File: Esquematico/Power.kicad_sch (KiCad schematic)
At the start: 5 parts, among them U1 AMS1117-3.3

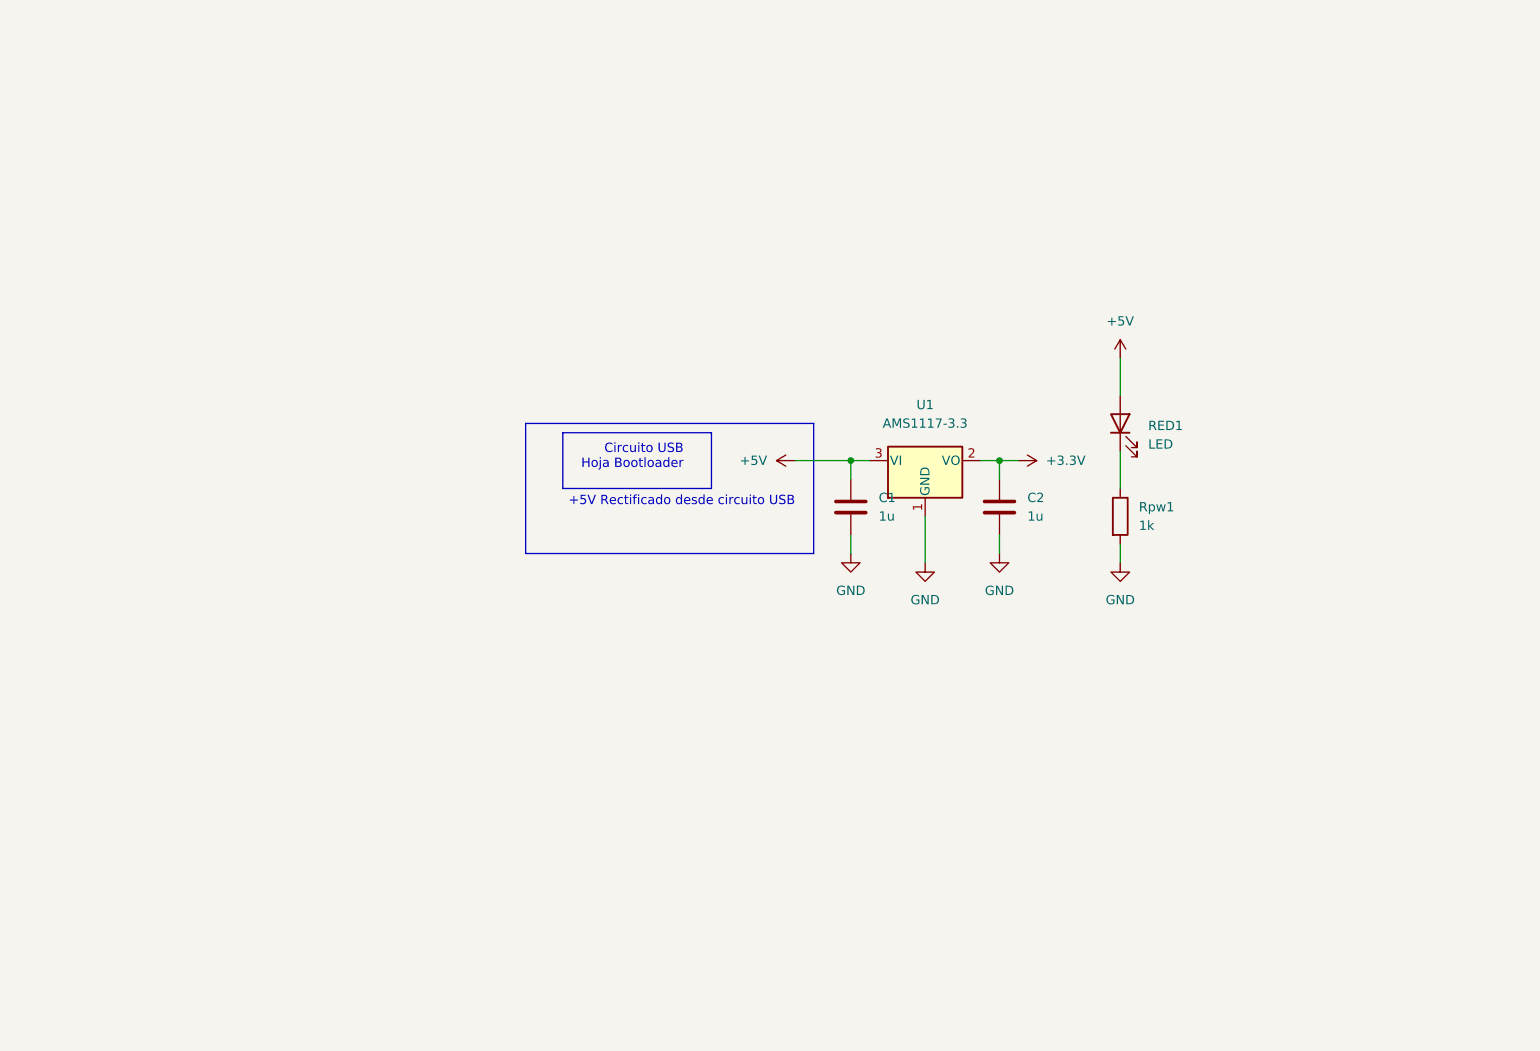
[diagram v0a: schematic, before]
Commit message: Agregado circuito de potencia a través de Jack y selector de posición para alimentar de USB, Jack o apagar
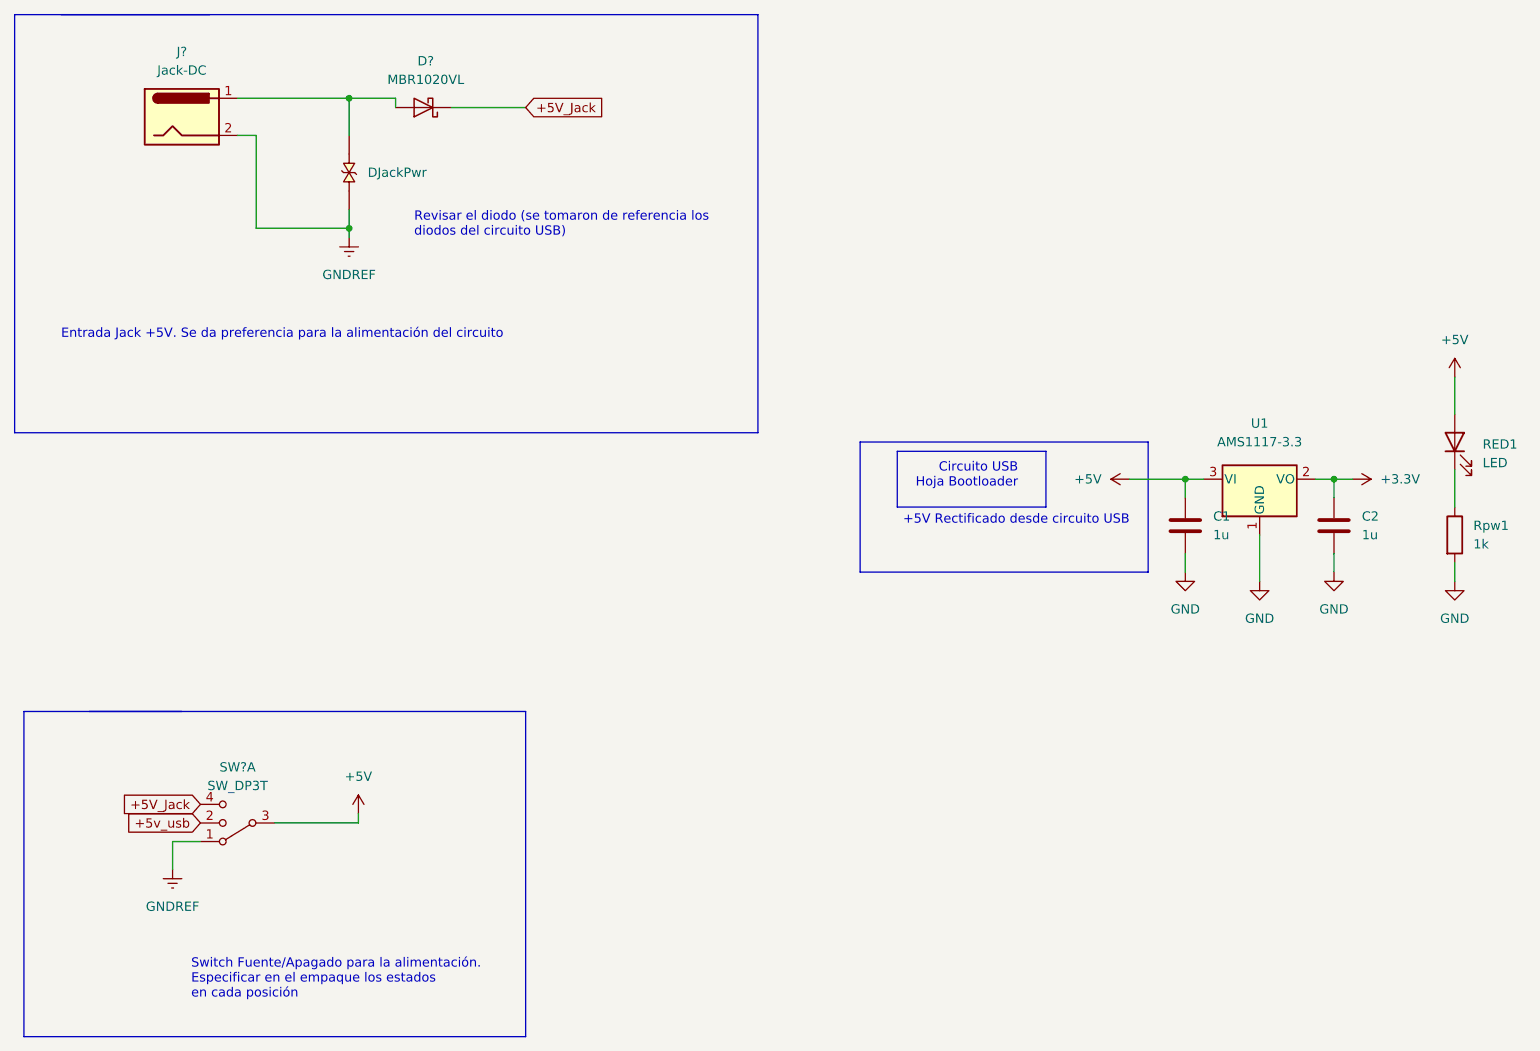
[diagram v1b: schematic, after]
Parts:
- added D?: MBR1020VL, Diode_SMD:D_SOD-123F, symbol Diode:MBR1020VL
- added DJackPwr: LESD5D5.0CT1G, TVS_LESD5D5.0CT1G, symbol LESD5D5.0CT1G:LESD5D5.0CT1G
- added J?: Jack-DC, symbol Connector:Jack-DC
- added SW?: SW_DP3T, symbol Switch:SW_DP3T
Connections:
- net +5V: now also SW?.3
- new net: D?.2 (A), DJackPwr.2, J?.1
- new net +5V_Jack: D?.1 (K), SW?.4
- new net +5v_usb: SW?.2
- new net GNDREF: DJackPwr.1, J?.2, SW?.1
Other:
- note added: "Entrada Jack +5V. Se da preferencia para la alimentación del circuito"
- note added: "Revisar el diodo (se tomaron de referencia los diodos del circuito USB)"
- note added: "Switch Fuente/Apagado para la alimentación. Especificar en el empaque los estados en cada posición"
- moved on the sheet: C1, C2, RED1, Rpw1, U1

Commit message: actualizacion huellas resitencias y capacitorees
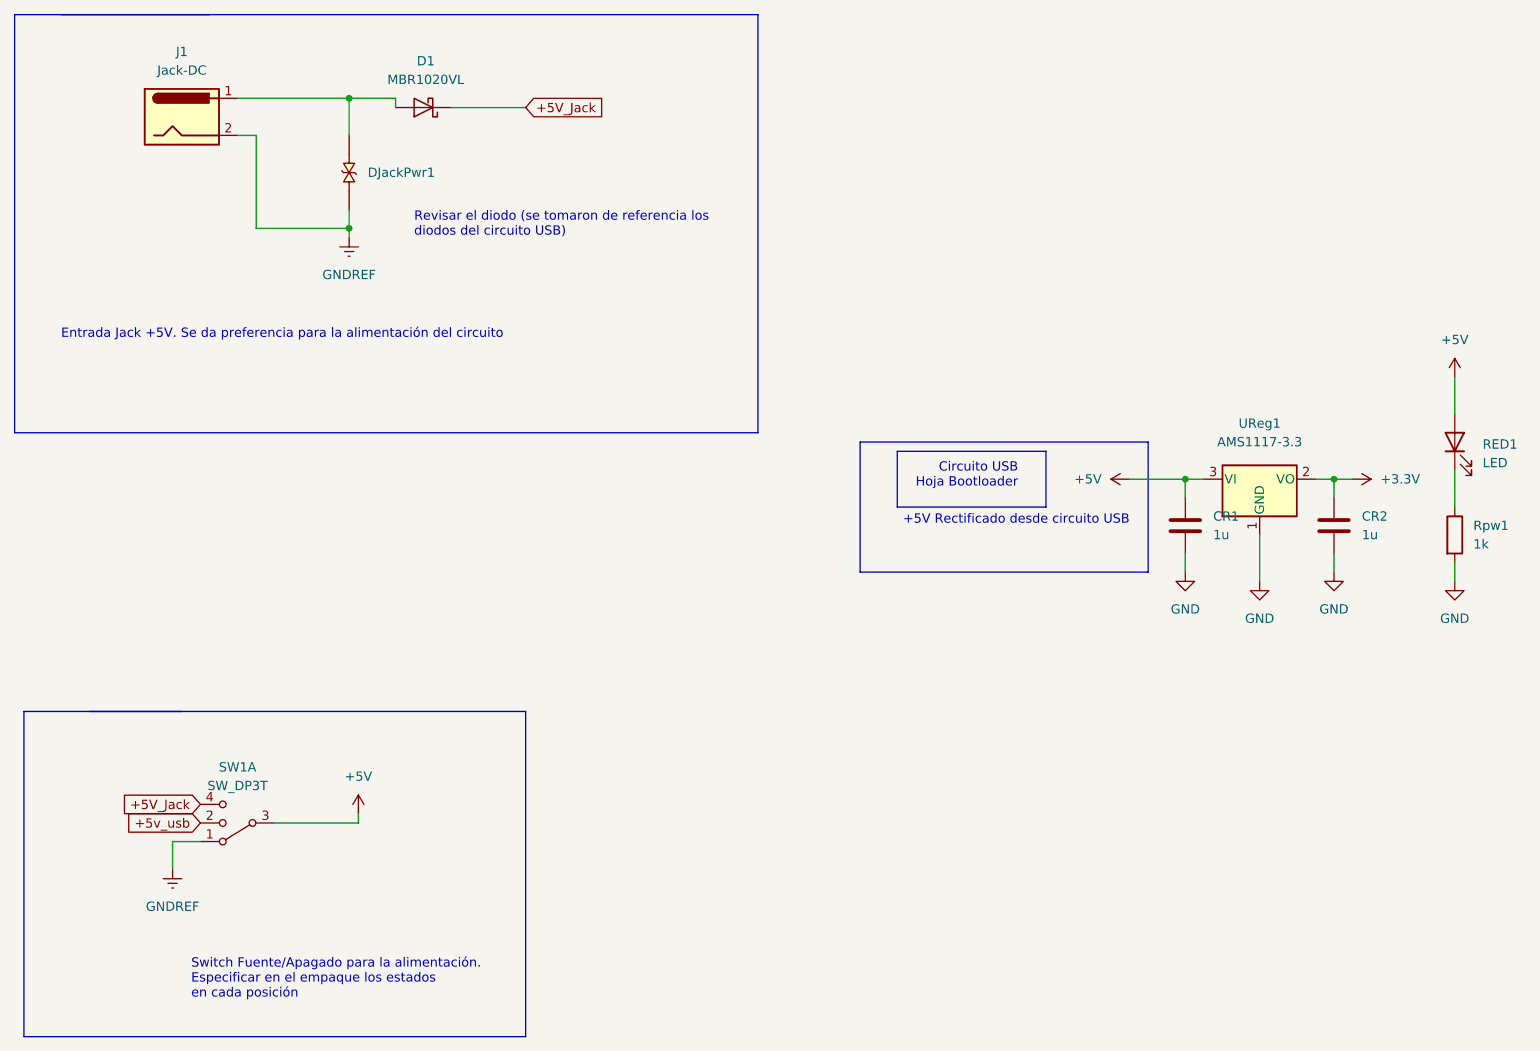
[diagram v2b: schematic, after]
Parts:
- CR1: renamed from C1; footprint (none) -> Capacitor_SMD:C_0805_2012Metric_Pad1.18x1.45mm_HandSolder
- CR2: renamed from C2; footprint (none) -> Capacitor_SMD:C_0805_2012Metric_Pad1.18x1.45mm_HandSolder
- DJackPwr1: renamed from DJackPwr; footprint TVS_LESD5D5.0CT1G -> LESD5D5:TVS_LESD5D5.0CT1G
- J1: renamed from J?; footprint (none) -> Connector_BarrelJack:BarrelJack_Horizontal
- RED1, Rpw1: footprint (none) -> Resistor_SMD:R_0805_2012Metric_Pad1.20x1.40mm_HandSolder
- gave numbers to parts that had none: 2
- renumbered U1 to UReg1
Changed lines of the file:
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@@
   (symbol (lib_id "power:GNDREF") (at 62.23 60.96 0) (unit 1)
     (in_bom yes) (on_board yes) (fields_autoplaced)
-    (property "Reference" "#PWR?" (id 0) (at 62.23 67.31 0)
+    (property "Reference" "#PWR0118" (id 0) (at 62.23 67.31 0)
       (effects (font (size 1.27 1.27)) hide)
     )
@@
   (symbol (lib_id "Switch:SW_DP3T") (at 46.99 140.97 180) (unit 1)
     (in_bom yes) (on_board yes) (fields_autoplaced)
-    (property "Reference" "SW?" (id 0) (at 46.99 133.35 0))
+    (property "Reference" "SW1" (id 0) (at 46.99 133.35 0))
     (property "Value" "SW_DP3T" (id 1) (at 46.99 135.89 0))
     (property "Footprint" "" (id 2) (at 62.865 145.415 0)
@@
   (symbol (lib_id "Device:C") (at 176.53 100.33 0) (unit 1)
     (in_bom yes) (on_board yes) (fields_autoplaced)
-    (property "Reference" "C1" (id 0) (at 180.34 99.0599 0)
+    (property "Reference" "CR1" (id 0) (at 180.34 99.0599 0)
       (effects (font (size 1.27 1.27)) (justify left))
     )
@@
       (effects (font (size 1.27 1.27)) (justify left))
     )
-    (property "Footprint" "" (id 2) (at 177.4952 104.14 0)
+    (property "Footprint" "Capacitor_SMD:C_0805_2012Metric_Pad1.18x1.45mm_HandSolder" (id 2) (at 177.4952 104.14 0)
       (effects (font (size 1.27 1.27)) hide)
     )
@@
   (symbol (lib_id "Diode:MBR1020VL") (at 72.39 43.18 180) (unit 1)
     (in_bom yes) (on_board yes) (fields_autoplaced)
-    (property "Reference" "D?" (id 0) (at 72.7075 36.83 0))
+    (property "Reference" "D1" (id 0) (at 72.7075 36.83 0))
     (property "Value" "MBR1020VL" (id 1) (at 72.7075 39.37 0))
     (property "Footprint" "Diode_SMD:D_SOD-123F" (id 2) (at 72.39 38.735 0)
@@
       (effects (font (size 1.27 1.27)) (justify right))
     )
-    (property "Footprint" "" (id 2) (at 213.36 88.9 0)
+    (property "Footprint" "Resistor_SMD:R_0805_2012Metric_Pad1.20x1.40mm_HandSolder" (id 2) (at 213.36 88.9 0)
       (effects (font (size 1.27 1.27)) hide)
     )
@@
   (symbol (lib_id "Regulator_Linear:AMS1117-3.3") (at 186.69 93.98 0) (unit 1)
     (in_bom yes) (on_board yes) (fields_autoplaced)
-    (property "Reference" "U1" (id 0) (at 186.69 86.36 0))
+    (property "Reference" "UReg1" (id 0) (at 186.69 86.36 0))
     (property "Value" "AMS1117-3.3" (id 1) (at 186.69 88.9 0))
     (property "Footprint" "Package_TO_SOT_SMD:SOT-223-3_TabPin2" (id 2) (at 186.69 88.9 0)
@@
       (effects (font (size 1.27 1.27)) (justify left))
     )
-    (property "Footprint" "" (id 2) (at 211.582 101.6 90)
+    (property "Footprint" "Resistor_SMD:R_0805_2012Metric_Pad1.20x1.40mm_HandSolder" (id 2) (at 211.582 101.6 90)
       (effects (font (size 1.27 1.27)) hide)
     )
@@
   (symbol (lib_id "power:+5V") (at 63.5 139.7 0) (unit 1)
     (in_bom yes) (on_board yes) (fields_autoplaced)
-    (property "Reference" "#PWR?" (id 0) (at 63.5 143.51 0)
+    (property "Reference" "#PWR0116" (id 0) (at 63.5 143.51 0)
       (effects (font (size 1.27 1.27)) hide)
     )
@@
   (symbol (lib_id "LESD5D5.0CT1G:LESD5D5.0CT1G") (at 62.23 52.07 90) (unit 1)
     (in_bom yes) (on_board yes) (fields_autoplaced)
-    (property "Reference" "DJackPwr" (id 0) (at 64.77 52.0699 90)
+    (property "Reference" "DJackPwr1" (id 0) (at 64.77 52.0699 90)
       (effects (font (size 1.27 1.27)) (justify right))
     )
@@
       (effects (font (size 1.27 1.27)) (justify right) hide)
     )
-    (property "Footprint" "TVS_LESD5D5.0CT1G" (id 2) (at 62.23 52.07 0)
+    (property "Footprint" "LESD5D5:TVS_LESD5D5.0CT1G" (id 2) (at 62.23 52.07 0)
       (effects (font (size 1.27 1.27)) (justify left bottom) hide)
     )
@@
   (symbol (lib_id "power:GNDREF") (at 38.1 147.32 0) (unit 1)
     (in_bom yes) (on_board yes) (fields_autoplaced)
-    (property "Reference" "#PWR?" (id 0) (at 38.1 153.67 0)
+    (property "Reference" "#PWR0117" (id 0) (at 38.1 153.67 0)
       (effects (font (size 1.27 1.27)) hide)
     )
@@
   (symbol (lib_id "Connector:Jack-DC") (at 39.37 44.45 0) (unit 1)
     (in_bom yes) (on_board yes) (fields_autoplaced)
-    (property "Reference" "J?" (id 0) (at 39.37 35.56 0))
+    (property "Reference" "J1" (id 0) (at 39.37 35.56 0))
     (property "Value" "Jack-DC" (id 1) (at 39.37 38.1 0))
-    (property "Footprint" "" (id 2) (at 40.64 45.466 0)
+    (property "Footprint" "Connector_BarrelJack:BarrelJack_Horizontal" (id 2) (at 40.64 45.466 0)
       (effects (font (size 1.27 1.27)) hide)
     )
@@
   (symbol (lib_id "Device:C") (at 196.85 100.33 0) (unit 1)
     (in_bom yes) (on_board yes) (fields_autoplaced)
-    (property "Reference" "C2" (id 0) (at 200.66 99.0599 0)
+    (property "Reference" "CR2" (id 0) (at 200.66 99.0599 0)
       (effects (font (size 1.27 1.27)) (justify left))
     )
@@
       (effects (font (size 1.27 1.27)) (justify left))
     )
-    (property "Footprint" "" (id 2) (at 197.8152 104.14 0)
-      (effects (font (size 1.27 1.27)) hide)
-    )
+    (property "Footprint" "Capacitor_SMD:C_0805_2012Metric_Pad1.18x1.45mm_HandSolder" (id 2) (at 197.8152 104.14 0)
+      (effects (font (size 1.27 1.27)) hide)
+    )
